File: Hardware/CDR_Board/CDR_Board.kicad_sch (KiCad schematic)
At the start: 59 parts, among them J1 BLE Friend, J2 nRF24L01, J3 Battery, J5 USB_C_Receptacle_USB2.0, Q1 DMP2045U, SW1 BOOTSEL, SW2 RESET, U1 W25Q32JVSS, U2 SOT23-5 200mA 3.3V, U3 RP2040, U4 BQ25172, U6 ADXL343, Y1 Crystal

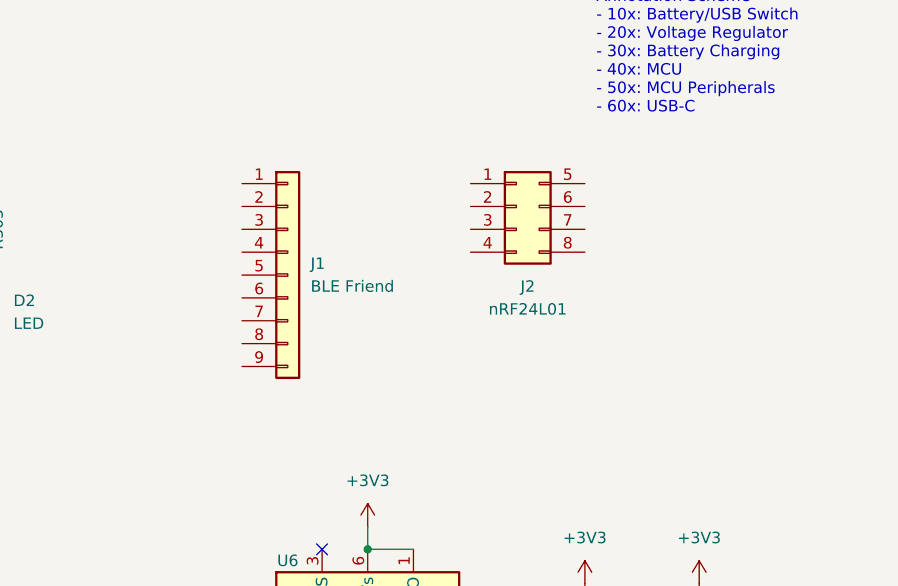
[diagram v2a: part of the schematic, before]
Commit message: Added critical traces
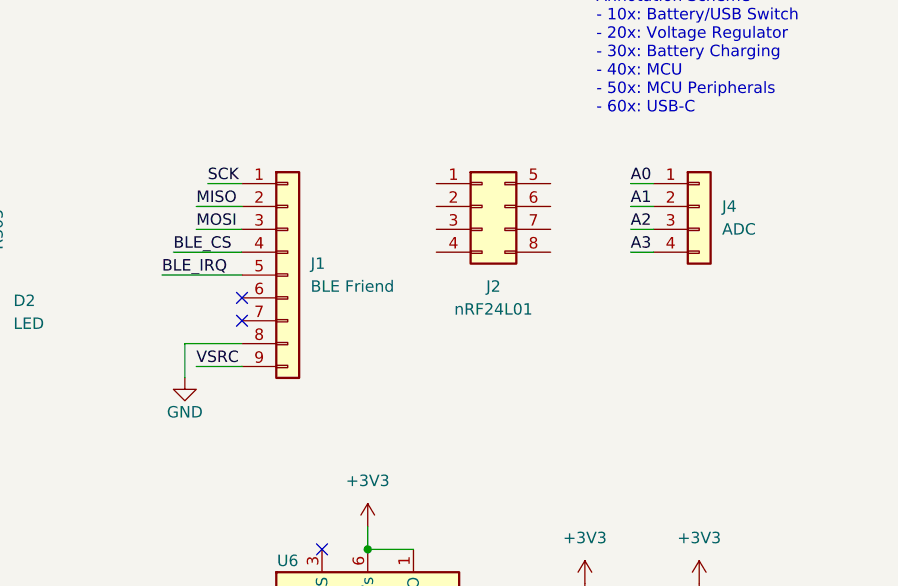
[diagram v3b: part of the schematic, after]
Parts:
- added J4: ADC, Connector_PinSocket_2.54mm:PinSocket_1x04_P2.54mm_Vertical, symbol Connector_Generic:Conn_01x04
- U3: footprint Package_DFN_QFN:QFN-56-1EP_7x7mm_P0.4mm_EP3.2x3.2mm_ThermalVias -> Package_DFN_QFN:QFN-56-1EP_7x7mm_P0.4mm_EP3.2x3.2mm
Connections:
- net A0: now also J4.1 (Pin_1)
- net A1: now also J4.2 (Pin_2)
- net A2: now also J4.3 (Pin_3)
- net A3: now also J4.4 (Pin_4)
- net GND: now also J1.8 (Pin_8)
- net MISO: now also J1.2 (Pin_2)
- net MOSI: now also J1.3 (Pin_3)
- net SCK: now also J1.1 (Pin_1)
- net VSRC: now also J1.9 (Pin_9)
- net BLE_CS: now reaches J1.4 (Pin_4)
- net BLE_IRQ: now reaches J1.5 (Pin_5)
- no-connect marks 17 -> 19
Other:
- moved on the sheet: J2
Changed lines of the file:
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@@
   (no_connect (at 217.17 96.52))
   (no_connect (at 217.17 88.9))
+  (no_connect (at 215.9 50.8))
+  (no_connect (at 215.9 53.34))
   (no_connect (at 234.95 104.14))
   (no_connect (at 224.79 78.74))
@@
     (stroke (width 0) (type default) (color 0 0 0 0))
   )
+  (wire (pts (xy 209.55 55.88) (xy 209.55 59.69))
+    (stroke (width 0) (type default) (color 0 0 0 0))
+  )
   (wire (pts (xy 179.07 97.79) (xy 179.07 100.33))
     (stroke (width 0) (type default) (color 0 0 0 0))
@@
     (stroke (width 0) (type default) (color 0 0 0 0))
   )
+  (wire (pts (xy 210.82 43.18) (xy 215.9 43.18))
+    (stroke (width 0) (type default) (color 0 0 0 0))
+  )
   (wire (pts (xy 105.41 96.52) (xy 107.95 96.52))
     (stroke (width 0) (type default) (color 0 0 0 0))
@@
     (stroke (width 0) (type default) (color 0 0 0 0))
   )
+  (wire (pts (xy 212.09 38.1) (xy 215.9 38.1))
+    (stroke (width 0) (type default) (color 0 0 0 0))
+  )
   (wire (pts (xy 93.98 38.1) (xy 93.98 39.37))
     (stroke (width 0) (type default) (color 0 0 0 0))
@@
     (stroke (width 0) (type default) (color 0 0 0 0))
   )
+  (wire (pts (xy 259.08 45.72) (xy 261.62 45.72))
+    (stroke (width 0) (type default) (color 0 0 0 0))
+  )
+  (wire (pts (xy 210.82 58.42) (xy 215.9 58.42))
+    (stroke (width 0) (type default) (color 0 0 0 0))
+  )
   (wire (pts (xy 135.89 180.34) (xy 144.78 180.34))
     (stroke (width 0) (type default) (color 0 0 0 0))
@@
     (stroke (width 0) (type default) (color 0 0 0 0))
   )
+  (wire (pts (xy 215.9 55.88) (xy 209.55 55.88))
+    (stroke (width 0) (type default) (color 0 0 0 0))
+  )
   (wire (pts (xy 118.11 96.52) (xy 120.65 96.52))
     (stroke (width 0) (type default) (color 0 0 0 0))
@@
     (stroke (width 0) (type default) (color 0 0 0 0))
   )
+  (wire (pts (xy 259.08 43.18) (xy 261.62 43.18))
+    (stroke (width 0) (type default) (color 0 0 0 0))
+  )
   (wire (pts (xy 148.59 85.09) (xy 156.21 85.09))
     (stroke (width 0) (type default) (color 0 0 0 0))
@@
     (stroke (width 0) (type default) (color 0 0 0 0))
   )
+  (wire (pts (xy 208.28 45.72) (xy 215.9 45.72))
+    (stroke (width 0) (type default) (color 0 0 0 0))
+  )
   (wire (pts (xy 105.41 96.52) (xy 105.41 85.09))
     (stroke (width 0) (type default) (color 0 0 0 0))
@@
     (stroke (width 0) (type default) (color 0 0 0 0))
   )
+  (wire (pts (xy 210.82 40.64) (xy 215.9 40.64))
+    (stroke (width 0) (type default) (color 0 0 0 0))
+  )
   (wire (pts (xy 40.64 109.22) (xy 40.64 110.49))
     (stroke (width 0) (type default) (color 0 0 0 0))
@@
     (stroke (width 0) (type default) (color 0 0 0 0))
   )
+  (wire (pts (xy 259.08 38.1) (xy 261.62 38.1))
+    (stroke (width 0) (type default) (color 0 0 0 0))
+  )
   (wire (pts (xy 247.65 138.43) (xy 247.65 140.97))
     (stroke (width 0) (type default) (color 0 0 0 0))
@@
     (stroke (width 0) (type default) (color 0 0 0 0))
   )
+  (wire (pts (xy 259.08 40.64) (xy 261.62 40.64))
+    (stroke (width 0) (type default) (color 0 0 0 0))
+  )
   (wire (pts (xy 247.65 135.89) (xy 251.46 135.89))
     (stroke (width 0) (type default) (color 0 0 0 0))
@@
   )
   (wire (pts (xy 245.11 125.73) (xy 247.65 125.73))
+    (stroke (width 0) (type default) (color 0 0 0 0))
+  )
+  (wire (pts (xy 207.01 48.26) (xy 215.9 48.26))
     (stroke (width 0) (type default) (color 0 0 0 0))
   )
@@
     (effects (font (size 1.27 1.27)) (justify right bottom))
   )
+  (label "A1" (at 259.08 40.64 0)
+    (effects (font (size 1.27 1.27)) (justify left bottom))
+  )
   (label "MISO" (at 144.78 157.48 180)
     (effects (font (size 1.27 1.27)) (justify right bottom))
@@
     (effects (font (size 1.27 1.27)) (justify left bottom))
   )
+  (label "BLE_IRQ" (at 207.01 48.26 0)
+    (effects (font (size 1.27 1.27)) (justify left bottom))
+  )
+  (label "BLE_CS" (at 208.28 45.72 0)
+    (effects (font (size 1.27 1.27)) (justify left bottom))
+  )
   (label "D11" (at 144.78 134.62 180)
     (effects (font (size 1.27 1.27)) (justify right bottom))
@@
     (effects (font (size 1.27 1.27)) (justify left bottom))
   )
+  (label "MOSI" (at 210.82 43.18 0)
+    (effects (font (size 1.27 1.27)) (justify left bottom))
+  )
+  (label "SCK" (at 212.09 38.1 0)
+    (effects (font (size 1.27 1.27)) (justify left bottom))
+  )
   (label "D10" (at 144.78 132.08 180)
     (effects (font (size 1.27 1.27)) (justify right bottom))
@@
     (effects (font (size 1.27 1.27)) (justify right bottom))
   )
+  (label "MISO" (at 210.82 40.64 0)
+    (effects (font (size 1.27 1.27)) (justify left bottom))
+  )
+  (label "A3" (at 259.08 45.72 0)
+    (effects (font (size 1.27 1.27)) (justify left bottom))
+  )
   (label "RUN" (at 175.26 135.89 180)
     (effects (font (size 1.27 1.27)) (justify right bottom))
@@
   )
   (label "XIN" (at 76.2 152.4 0)
+    (effects (font (size 1.27 1.27)) (justify left bottom))
+  )
+  (label "VSRC" (at 210.82 58.42 0)
+    (effects (font (size 1.27 1.27)) (justify left bottom))
+  )
+  (label "A0" (at 259.08 38.1 0)
+    (effects (font (size 1.27 1.27)) (justify left bottom))
+  )
+  (label "A2" (at 259.08 43.18 0)
     (effects (font (size 1.27 1.27)) (justify left bottom))
   )
@@
       (effects (font (size 1.27 1.27)) (justify left))
     )
-    (property "Footprint" "Package_DFN_QFN:QFN-56-1EP_7x7mm_P0.4mm_EP3.2x3.2mm_ThermalVias" (id 2) (at 110.49 144.78 0)
+    (property "Footprint" "Package_DFN_QFN:QFN-56-1EP_7x7mm_P0.4mm_EP3.2x3.2mm" (id 2) (at 110.49 144.78 0)
       (effects (font (size 1.27 1.27)) hide)
     )
@@
     (pin "2")
   )
+  (symbol (lib_id "power:GND") (at 209.55 59.69 0) (mirror y) (unit 1)
+    (in_bom yes) (on_board yes)
+    (property "Reference" "#PWR0105" (id 0) (at 209.55 66.04 0)
+      (effects (font (size 1.27 1.27)) hide)
+    )
+    (property "Value" "GND" (id 1) (at 209.55 63.5 0))
+    (property "Footprint" "" (id 2) (at 209.55 59.69 0)
+      (effects (font (size 1.27 1.27)) hide)
+    )
+    (property "Datasheet" "" (id 3) (at 209.55 59.69 0)
+      (effects (font (size 1.27 1.27)) hide)
+    )
+    (pin "1")
+  )
   (symbol (lib_id "power:GND") (at 59.69 87.63 0) (unit 1)
     (in_bom yes) (on_board yes)
@@
     )
     (pin "1")
+  )
+  (symbol (lib_id "Connector_Generic:Conn_01x04") (at 266.7 40.64 0) (unit 1)
+    (in_bom yes) (on_board yes)
+    (property "Reference" "J4" (id 0) (at 269.24 40.6399 0)
+      (effects (font (size 1.27 1.27)) (justify left))
+    )
+    (property "Value" "ADC" (id 1) (at 269.24 43.1799 0)
+      (effects (font (size 1.27 1.27)) (justify left))
+    )
+    (property "Footprint" "Connector_PinSocket_2.54mm:PinSocket_1x04_P2.54mm_Vertical" (id 2) (at 266.7 40.64 0)
+      (effects (font (size 1.27 1.27)) hide)
+    )
+    (property "Datasheet" "~" (id 3) (at 266.7 40.64 0)
+      (effects (font (size 1.27 1.27)) hide)
+    )
+    (pin "1")
+    (pin "2")
+    (pin "3")
+    (pin "4")
   )
   (symbol (lib_id "power:GND") (at 107.95 53.34 0) (unit 1)
@@
     (pin "2")
   )
-  (symbol (lib_id "Connector_Generic:Conn_02x04_Top_Bottom") (at 246.38 40.64 0) (unit 1)
-    (in_bom yes) (on_board yes)
-    (property "Reference" "J2" (id 0) (at 247.65 49.53 0))
-    (property "Value" "nRF24L01" (id 1) (at 247.65 52.07 0))
-    (property "Footprint" "Connector_PinSocket_2.54mm:PinSocket_2x04_P2.54mm_Vertical" (id 2) (at 246.38 40.64 0)
-      (effects (font (size 1.27 1.27)) hide)
-    )
-    (property "Datasheet" "~" (id 3) (at 246.38 40.64 0)
+  (symbol (lib_id "Connector_Generic:Conn_02x04_Top_Bottom") (at 242.57 40.64 0) (unit 1)
+    (in_bom yes) (on_board yes)
+    (property "Reference" "J2" (id 0) (at 243.84 49.53 0))
+    (property "Value" "nRF24L01" (id 1) (at 243.84 52.07 0))
+    (property "Footprint" "Connector_PinSocket_2.54mm:PinSocket_2x04_P2.54mm_Vertical" (id 2) (at 242.57 40.64 0)
+      (effects (font (size 1.27 1.27)) hide)
+    )
+    (property "Datasheet" "~" (id 3) (at 242.57 40.64 0)
       (effects (font (size 1.27 1.27)) hide)
     )
@@
       (reference "#PWR0104") (unit 1) (value "+BATT") (footprint "")
     )
+    (path "/27f47b4e-a078-4e45-b253-7bbd97aee0c6"
+      (reference "#PWR0105") (unit 1) (value "GND") (footprint "")
+    )
     (path "/25807b8f-3b59-4daa-8867-9de0e8d1d419"
       (reference "C201") (unit 1) (value "1u") (footprint "Capacitor_SMD:C_0805_2012Metric_Pad1.18x1.45mm_HandSolder")
@@
       (reference "J3") (unit 1) (value "Battery") (footprint "Connector_JST:JST_PH_S2B-PH-SM4-TB_1x02-1MP_P2.00mm_Horizontal")
     )
+    (path "/ab5e4019-1fbf-4d26-96e2-5c0ebd47fb45"
+      (reference "J4") (unit 1) (value "ADC") (footprint "Connector_PinSocket_2.54mm:PinSocket_1x04_P2.54mm_Vertical")
+    )
     (path "/1fa69909-b073-4946-b85a-788027220bc9"
       (reference "J5") (unit 1) (value "USB_C_Receptacle_USB2.0") (footprint "Connector_USB:USB_C_Receptacle_Palconn_UTC16-G")
@@
     )
     (path "/18ae02dd-23fd-4070-a605-96a6877ec73c"
-      (reference "U3") (unit 1) (value "RP2040") (footprint "Package_DFN_QFN:QFN-56-1EP_7x7mm_P0.4mm_EP3.2x3.2mm_ThermalVias")
+      (reference "U3") (unit 1) (value "RP2040") (footprint "Package_DFN_QFN:QFN-56-1EP_7x7mm_P0.4mm_EP3.2x3.2mm")
     )
     (path "/6001ccdb-cdbb-4e67-8219-bebe4e61292b"

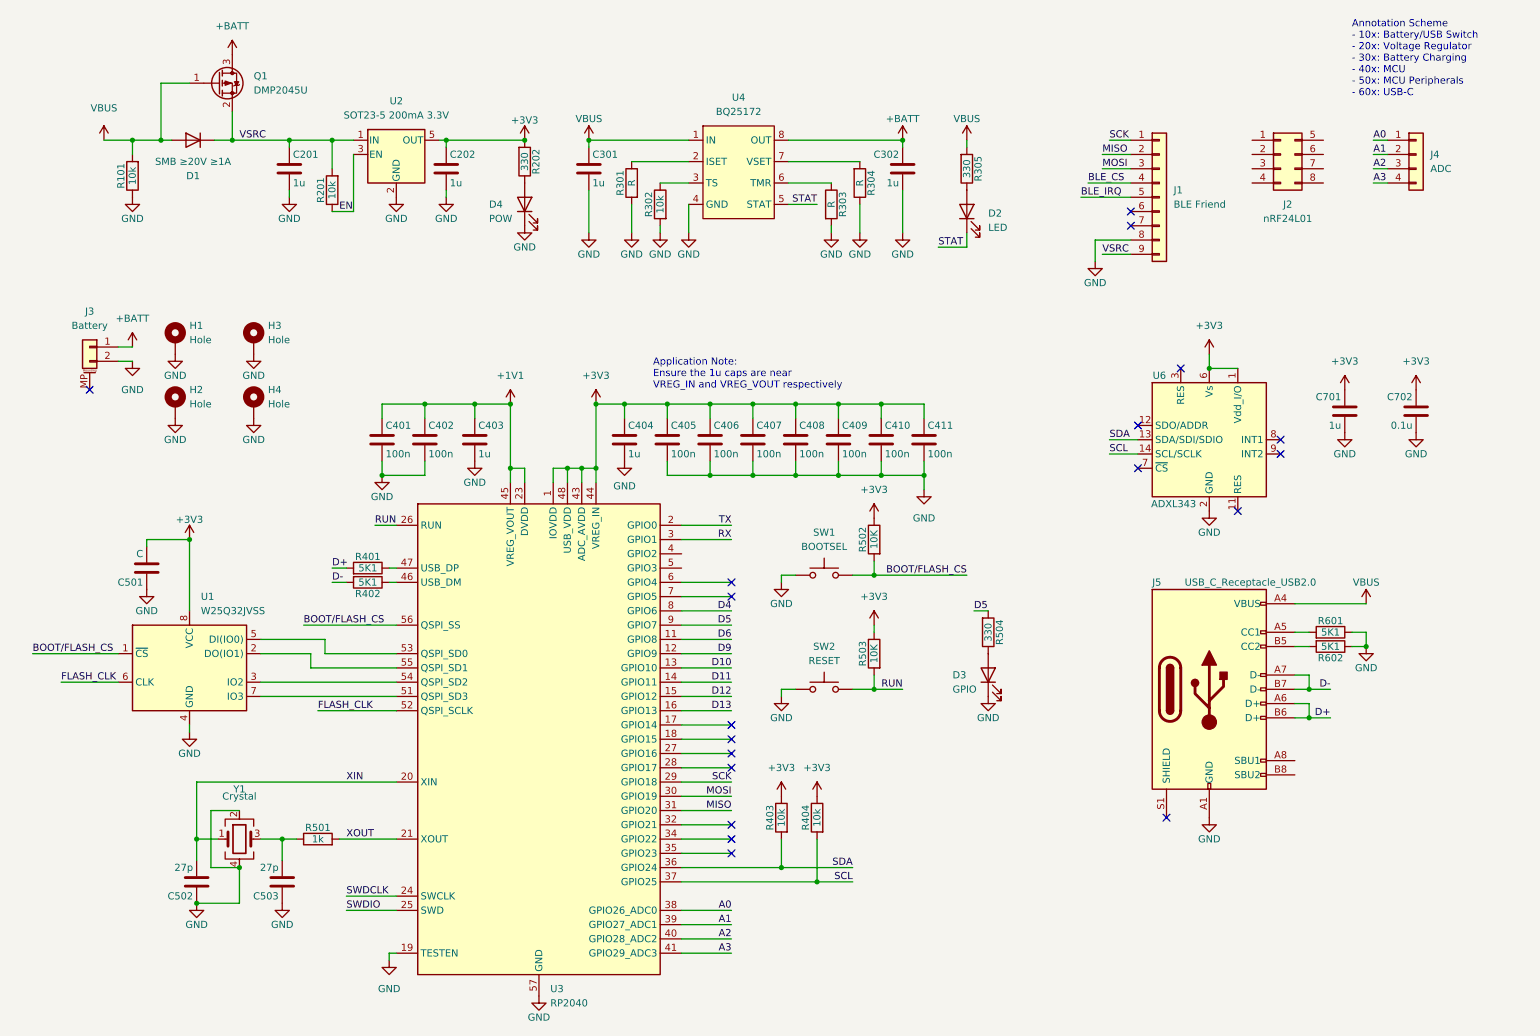
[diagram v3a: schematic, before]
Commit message: Finished all routing
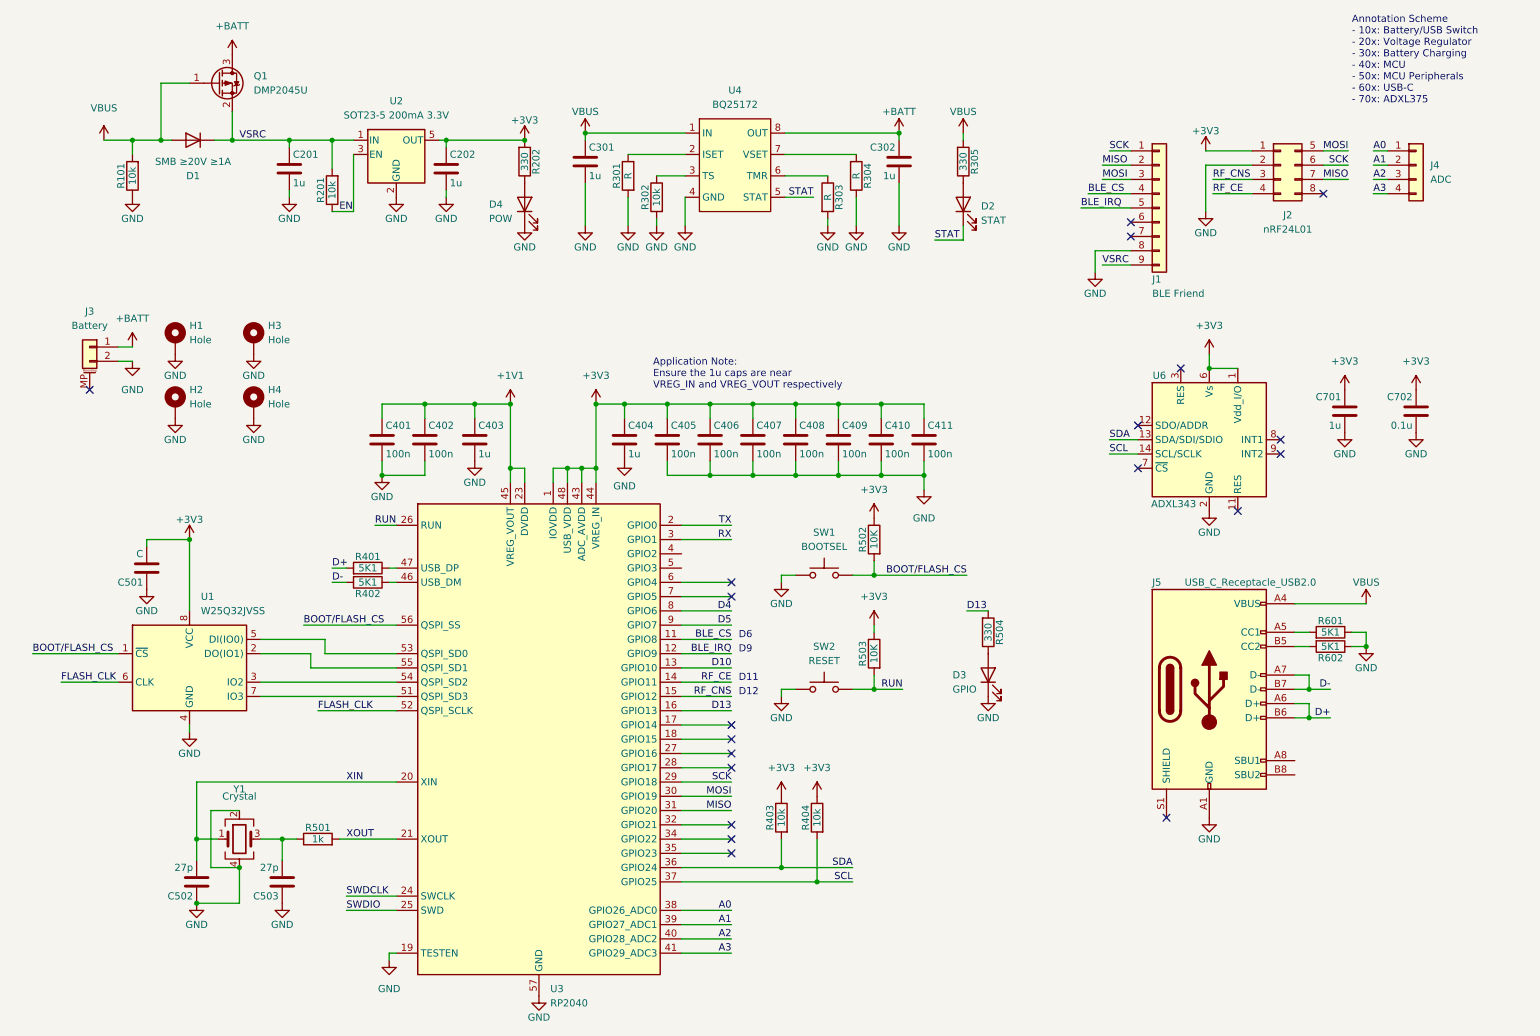
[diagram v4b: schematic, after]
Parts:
- D2: value LED -> STAT
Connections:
- net D11 is gone; now on net RF_CE: U3.14 (GPIO11)
- net D12 is gone; now on net RF_CNS: U3.15 (GPIO12)
- net D6 is gone; now on net BLE_CS: U3.11 (GPIO8)
- net D9 is gone; now on net BLE_IRQ: U3.12 (GPIO9)
- net +3V3: now also J2.1 (Pin_1)
- net D13: now also R504.2
- net D5: no longer R504.2
- net GND: now also J2.2 (Pin_2)
- net MISO: now also J2.7 (Pin_7)
- net MOSI: now also J2.5 (Pin_5)
- net SCK: now also J2.6 (Pin_6)
- net RF_CNS: now reaches J2.3 (Pin_3)
- net RF_CE: now reaches J2.4 (Pin_4)
- no-connect marks 19 -> 20
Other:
- note added: "Annotation Scheme - 10x: Battery/USB Switch - 20x: Voltage Regulator - 30x: Battery Charging - 40x: MCU - 50x: MCU Peripherals - 60x: USB-C - 70x: ADXL375"
- note added: "D11"
- note added: "D12"
- note added: "D6"
- note added: "D9"
- note removed: "Annotation Scheme - 10x: Battery/USB Switch - 20x: Voltage Regulator - 30x: Battery Charging - 40x: MCU - 50x: MCU Peripherals - 60x: USB-C"
- moved on the sheet: C301, C302, D2, J1, J2, J4, R301, R302, R303, R304, R305, U4
